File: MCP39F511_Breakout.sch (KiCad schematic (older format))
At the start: 1 part

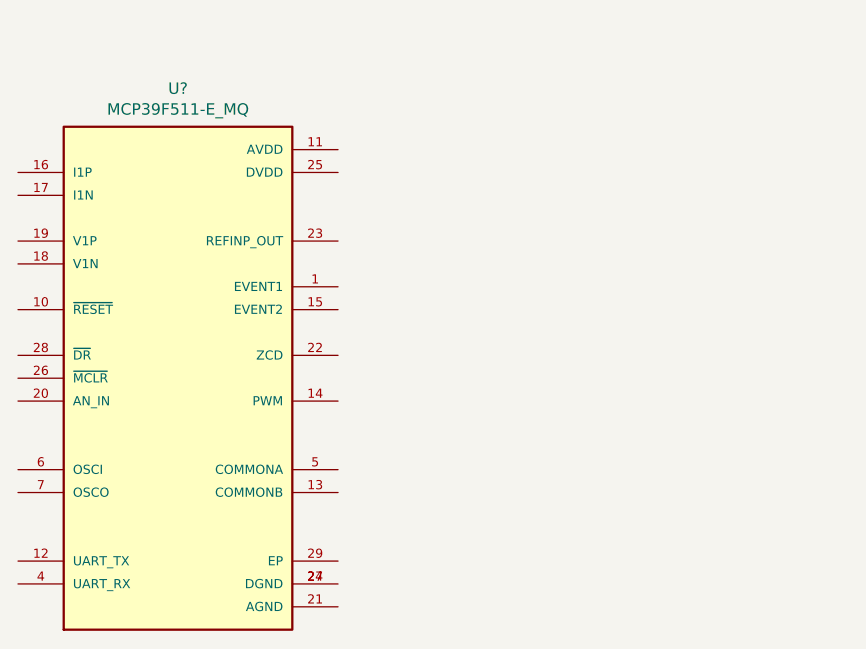
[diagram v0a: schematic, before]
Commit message: PCB Edge cuts
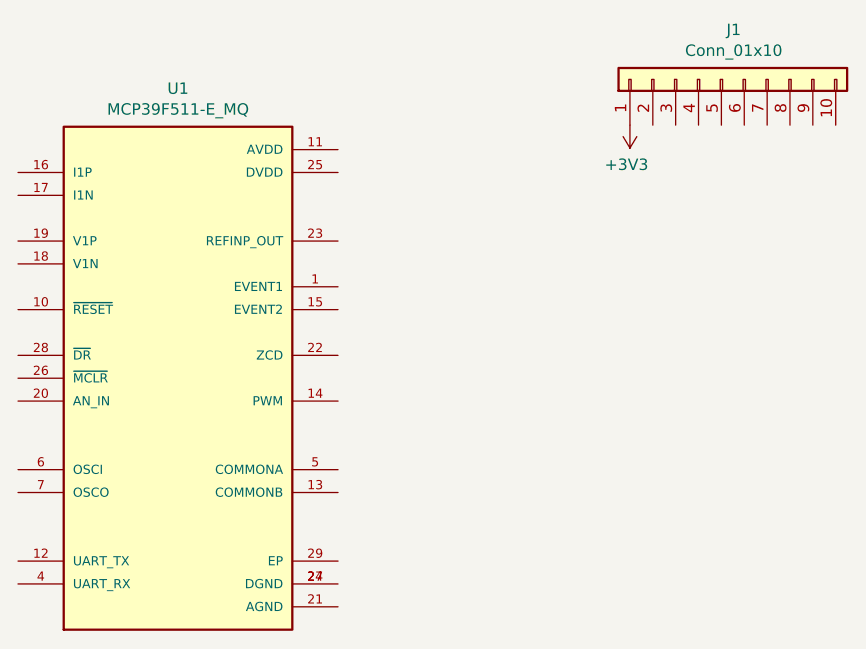
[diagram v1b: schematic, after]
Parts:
- added J1: Conn_01x10, Connector_PinHeader_2.54mm:PinHeader_1x10_P2.54mm_Vertical, symbol Connector_Generic:Conn_01x10
- U1: renamed from U?; footprint QFN50P500X500X100-29N -> mcp39f511:QFN50P500X500X100-29N
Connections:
- new net +3V3: J1.1 (Pin_1)
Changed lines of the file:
@@
 $EndDescr
 $Comp
-L MCP39F511-E_MQ:MCP39F511-E_MQ U?
+L MCP39F511-E_MQ:MCP39F511-E_MQ U1
 U 1 1 5FAE364E
 P 5276 3271
-F 0 "U?" H 5276 4538 50  0000 C CNN
+F 0 "U1" H 5276 4538 50  0000 C CNN
 F 1 "MCP39F511-E_MQ" H 5276 4447 50  0000 C CNN
-F 2 "QFN50P500X500X100-29N" H 5276 3271 50  0001 L BNN
+F 2 "mcp39f511:QFN50P500X500X100-29N" H 5276 3271 50  0001 L BNN
 F 3 "" H 5276 3271 50  0001 L BNN
 F 4 "B" H 5276 3271 50  0001 L BNN "PARTREV"
@@
 	1    0    0    -1
 $EndComp
+$Comp
+L Connector_Generic:Conn_01x10 J1
+U 1 1 5FAE805E
+P 7653 1964
+F 0 "J1" V 7870 1910 50  0000 C CNN
+F 1 "Conn_01x10" V 7779 1910 50  0000 C CNN
+F 2 "Connector_PinHeader_2.54mm:PinHeader_1x10_P2.54mm_Vertical" H 7653 1964 50  0001 C CNN
+F 3 "~" H 7653 1964 50  0001 C CNN
+	1    7653 1964
+	0    -1   -1   0
+$EndComp
+$Comp
+L power:+3V3 #PWR?
+U 1 1 5FAE9069
+P 7253 2164
+F 0 "#PWR?" H 7253 2014 50  0001 C CNN
+F 1 "+3V3" H 7268 2337 50  0000 C CNN
+F 2 "" H 7253 2164 50  0001 C CNN
+F 3 "" H 7253 2164 50  0001 C CNN
+	1    7253 2164
+	-1   0    0    1
+$EndComp
 $EndSCHEMATC
